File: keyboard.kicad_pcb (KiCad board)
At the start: 2 copper layers, 285 x 94.6 mm, 205 parts, among them J1 USB_OTG, K1 Jumper_NO_Small, P1 SWD, P2 BATT, U1 nrf51822-02, U2 CH554T, U3 TP4057, U4 XC6206P30

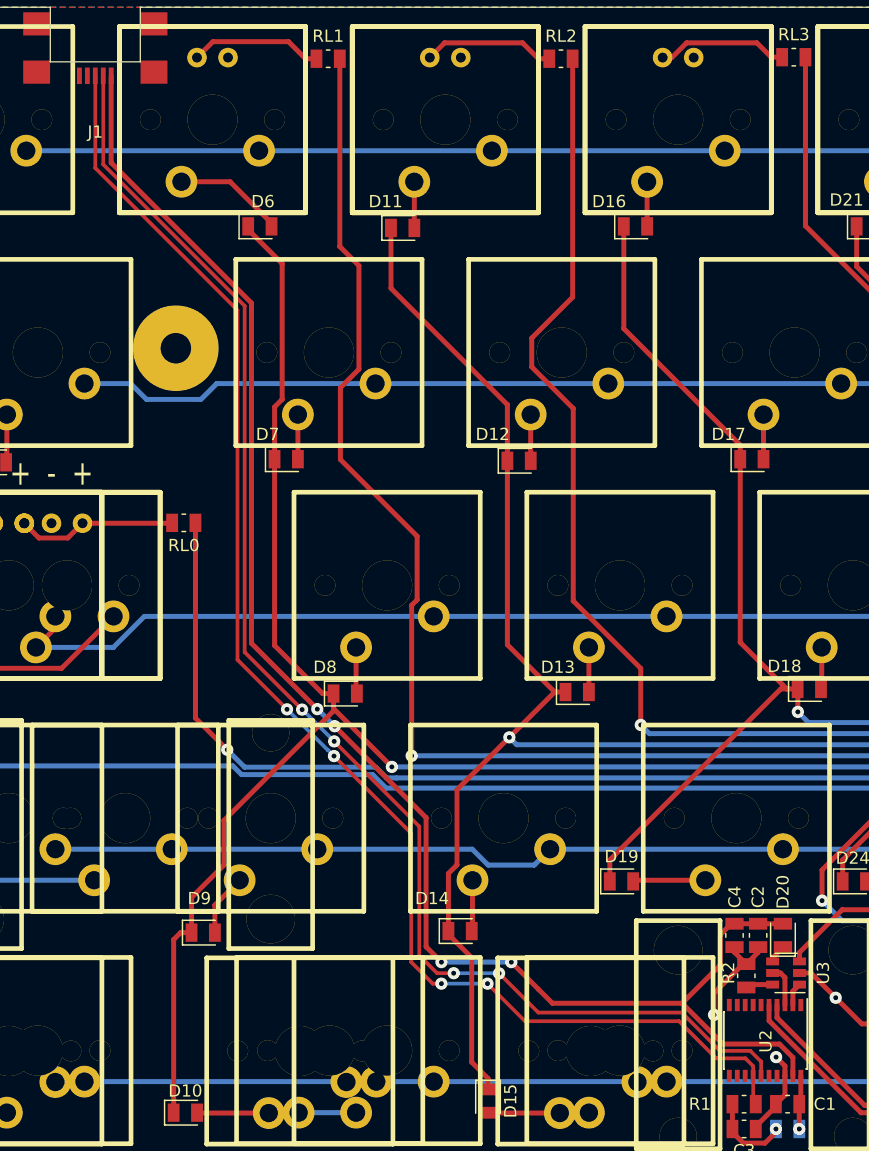
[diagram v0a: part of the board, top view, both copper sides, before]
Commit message: 应该是改了些布线方面的问题
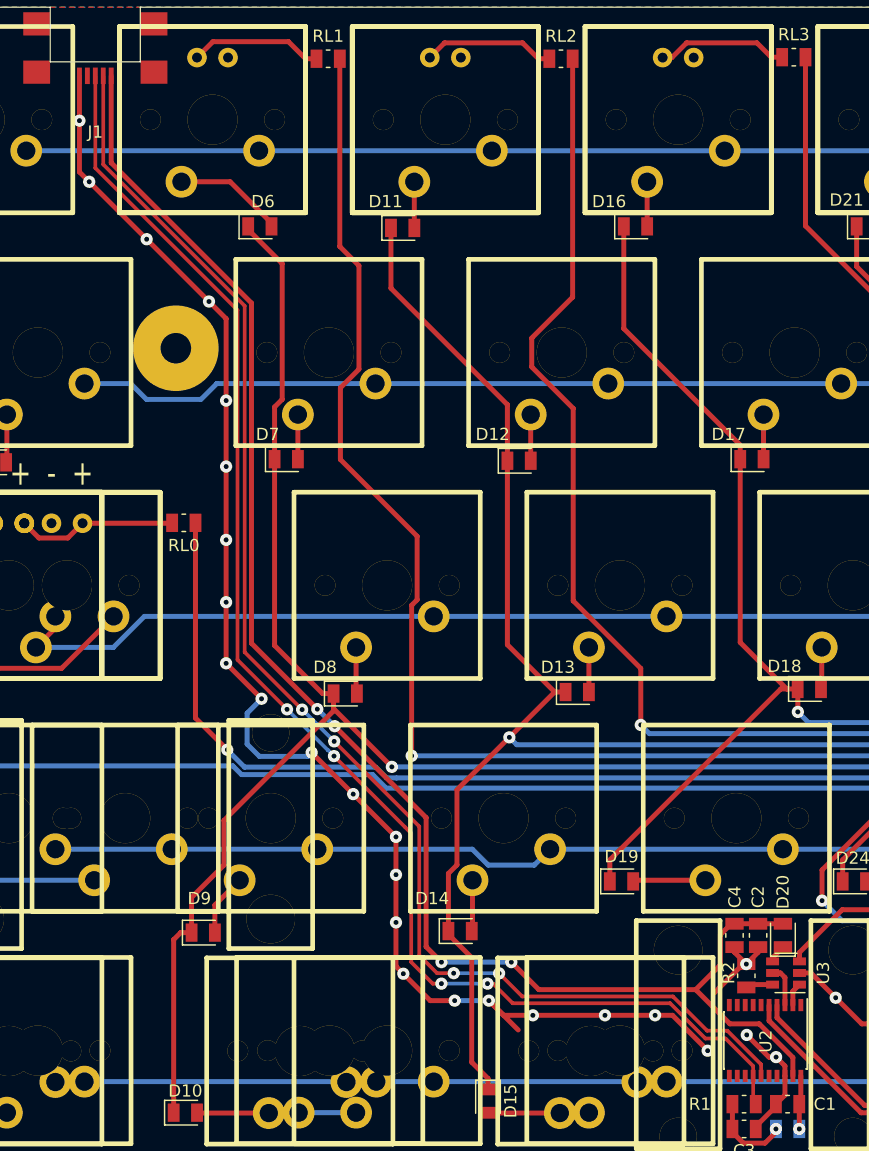
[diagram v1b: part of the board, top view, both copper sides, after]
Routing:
- net GND: track 83.6 -> 204.3 mm, vias 5 -> 28
- net VCC: track 129.6 -> 128.1 mm

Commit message: 替换接口为Type-C
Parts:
- added R5: 5.1K, Resistor_SMD:R_0805_2012Metric, B.Cu at (74.2, 69.6)
- added R6: 5.1K, Resistor_SMD:R_0805_2012Metric, B.Cu at (78.9, 75.4)
- added TP1: TP, TestPoint:TestPoint_Pad_D1.0mm, B.Cu at (140.6, 146.9)
- added TP2: TP, TestPoint:TestPoint_Pad_D1.0mm, B.Cu at (143.8, 146.9)
- added TP3: TP, TestPoint:TestPoint_Pad_D1.0mm, B.Cu at (142.2, 146.9)
- C1, C3, D20, P1, R1, R2, U1, U2, U3: moved to B.Cu
- J1: value USB_OTG -> USB_C_Receptacle_USB2.0; footprint custom:USB_Micro-B_lowp -> Connector_USB:USB_C_Receptacle_Amphenol_12401610E4-2A; moved to B.Cu
- moved U1 17.9 mm to (179.4, 140.2), turned to 270 degrees
- moved C4 9.21 mm to (136.4, 149.2)
- moved C2 8.67 mm to (134.4, 149.2)
- moved P1 7.04 mm to (140.8, 153.4), turned to 270 degrees
- moved R1 3.62 mm to (137.6, 154.2), turned to 180 degrees
- moved C3 3.62 mm to (137.6, 156.4), turned to 180 degrees
- moved C1 3.59 mm to (134.0, 154.2), turned to 0 degrees
- moved K1 3.59 mm to (134.0, 156.4), turned to 180 degrees
- moved R2 3.44 mm to (133.8, 140.4)
- moved U3 3.39 mm to (136.4, 140.4), turned to 270 degrees
- moved J1 2.73 mm to (81.0, 68.2), turned to 0 degrees
- moved D20 2.25 mm to (139.4, 140.4)
- moved G*** 0.64 mm to (226.0, 151.0)
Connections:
- U1 pad 32: TXD -> MOSI
- U1 pad 33: RXD -> MISO
- U1 pad 34: Net-(U1-Pad34) -> CLK
- U2 pad 4: RXD -> MOSI
- U2 pad 5: TXD -> MISO
- U2 pad 7: Net-(U2-Pad7) -> CLK
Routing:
- net GND: track 204.3 -> 286.9 mm, vias 28 -> 30
- net MOSI: track 0.00 -> 47.8 mm
- net MISO: track 0.00 -> 45.3 mm
- net CLK: track 0.00 -> 41.6 mm
- net /row3: track 359.3 -> 319.6 mm
- net RXD: track 35.9 -> 0.00 mm
- net TXD: track 35.5 -> 0.00 mm
- net VCC: track 128.1 -> 158.1 mm, vias 4 -> 6
- net /col1: track 177.6 -> 198.3 mm, vias 2 -> 3
- net UD_N: track 115.3 -> 134.3 mm
- net /caps_led: track 99.5 -> 118.1 mm, vias 2 -> 3
- net /col6: track 79.4 -> 97.9 mm, vias 0 -> 1
- net /led3: track 87.0 -> 105.0 mm, vias 2 -> 3
- net /row4: track 332.8 -> 314.8 mm
- net /col4: track 108.9 -> 126.8 mm, vias 2 -> 3
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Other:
- net class DATA: clearance 0.2032 -> 0.15; trace_width 0.3048 -> 0.25; via_dia 1 -> 0.7
- rule via_min_drill: 0.4 -> 0.3
- rule via_min_size: 1 -> 0.6
- board text added: "Last Order"
- board text added: "Lot60-BLE Rev.C ©2019 Lotlab"
- board text removed: "Lot60-BLE Rev.A ©2018 Lotlab"

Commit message: 使用52810替换51822
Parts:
- removed LED4, LED5: LED, MX1A:MX1A-led
- removed RL4, RL5: R, Resistor_SMD:R_0805_2012Metric
- added C8: 10uF, Capacitor_SMD:C_0805_2012Metric, F.Cu at (137.9, 149.4)
- added J2: -, Connector_PinSocket_2.54mm:PinSocket_1x05_P2.54mm_Vertical, F.Cu at (63.9, 98.6)
- added J3: -, Connector_PinSocket_2.54mm:PinSocket_1x05_P2.54mm_Vertical, F.Cu at (154.3, 157.5)
- added JP1: Jumper, Jumper:SolderJumper-2_P1.3mm_Bridged2Bar_Pad1.0x1.5mm, B.Cu at (143.8, 150.0)
- added TP4: TP, TestPoint:TestPoint_Pad_D1.0mm, B.Cu at (140.6, 144.5)
- added TP5: TP, TestPoint:TestPoint_Pad_D1.0mm, B.Cu at (139.1, 144.5)
- C1, C3, K1, P1, R1: moved to F.Cu
- C4: value 1uF -> 0.1uF
- D1, D10, D11, D12, D13, D14, D15, D16, D17, D18, D19, D2, D21, D22, D23, D24, D26, D27, D28, D29, D3, D30, D31, D32, D33, D34, D36, D37, D38, D39, D4, D41, D42, D43, D44, D46, D47, D48, D49, D5, D50, D51, D52, D53, D54, D55, D56, D57, D58, D59, D6, D60, D61, D62, D63, D64, D65, D66, D67, D68, D69, D7, D70, D8, D9, P2, RL0: moved to B.Cu
- RL1, RL2, RL3: value R -> 4.7K; moved to B.Cu
- U1: value nrf51822-02 -> nRF52810-ND04C; footprint custom:nRF51822-02 -> Customv2:nRF52810-ND04C
- moved P1 31.5 mm to (172.1, 157.5)
- moved RL1 27.2 mm to (76.5, 82.7)
- moved D30 24.8 mm to (178.6, 155.1)
- moved D29 20.0 mm to (181.4, 136.9)
- moved RL2 19.1 mm to (99.9, 68.7)
- moved LED3 19.1 mm to (109.5, 73.8)
- moved LED2 19.1 mm to (90.5, 73.8)
- moved LED1 19.0 mm to (71.4, 73.8)
- moved RL3 19.0 mm to (119.0, 68.7)
- moved U1 8.80 mm to (174.1, 147.2), turned to 180 degrees
- moved R2 4.09 mm to (133.6, 144.5), turned to 180 degrees
- moved D6 3.64 mm to (90.7, 82.7)
- moved D15 1.70 mm to (113.1, 155.8), turned to 90 degrees
- moved R6 1.56 mm to (78.9, 77.0)
- moved D20 1.45 mm to (138.5, 141.5)
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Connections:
- RL0 pad 1: /caps_led -> /caps
- U1 pad 1: 3V3 -> GND
- U1 pad 10: /col7 -> /row4
- U1 pad 11: GND -> /row5
- U1 pad 12: /led5 -> /col7
- U1 pad 13: /col6 -> ADC1
- U1 pad 14: /led4 -> /col8
- U1 pad 15: /col5 -> /col9
- U1 pad 16: /led3 -> /col10
- U1 pad 17: /col4 -> /col11
- U1 pad 18: /led2 -> /col12
- U1 pad 19: /col3 -> /col13
- U1 pad 2: /col14 -> 3V3
- U1 pad 20: /led1 -> /col14
- U1 pad 21: DIO -> /GPIO0
- U1 pad 22: DCLK -> /col6
- U1 pad 23: /col2 -> /col5
- U1 pad 24: /caps_led -> /col4
- U1 pad 25: /col1 -> /col3
- U1 pad 26: Net-(U1-Pad26) -> /col2
- U1 pad 27: GND -> /col1
- U1 pad 28: Net-(U1-Pad28) -> DIO
- U1 pad 29: GND -> DCLK
- U1 pad 3: /col13 -> /caps
- U1 pad 30: GND -> CLK
- U1 pad 31: GND -> MISO
- U1 pad 32: MOSI -> /GPIO2
- U1 pad 33: MISO -> /GPIO1
- U1 pad 4: ADC1 -> /led1
- U1 pad 5: /col12 -> /led2
- U1 pad 6: /col11 -> /led3
- U1 pad 7: /col10 -> /row1
- U1 pad 8: /col9 -> /row2
- U1 pad 9: /col8 -> /row3
- U2 pad 10: Net-(U2-Pad10) -> D_RX
- U2 pad 11: Net-(U2-Pad11) -> CHRG
- U2 pad 12: Net-(U2-Pad12) -> STBY
- U2 pad 2: CHRG -> Net-(U2-Pad2)
- U2 pad 3: STBY -> MOSI
- U2 pad 4: MOSI -> MISO
- U2 pad 5: MISO -> CLK
- U2 pad 7: CLK -> Net-(U2-Pad7)
- U2 pad 9: Net-(U2-Pad9) -> D_TX
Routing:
- net /caps_led: track 118.1 -> 0.00 mm, vias 3 -> 0
- net /caps: track 0.00 -> 103.4 mm, vias 0 -> 2
- net /led4: track 95.3 -> 0.00 mm, vias 1 -> 0
- net /led5: track 94.3 -> 0.00 mm, vias 3 -> 0
- net /row1: track 422.4 -> 354.1 mm, vias 1 -> 0
- net /row5: track 385.8 -> 438.6 mm, vias 0 -> 3
- net GND: track 286.9 -> 336.0 mm, vias 30 -> 7
- net MOSI: track 47.8 -> 16.4 mm
- net /GPIO0: track 0.00 -> 25.3 mm
- net /GPIO2: track 0.00 -> 24.8 mm
- net Net-(D30-Pad2): track 44.8 -> 22.7 mm
- net DIO: track 26.2 -> 4.82 mm
- net /row3: track 319.6 -> 340.8 mm, vias 2 -> 0
- net DCLK: track 21.6 -> 3.68 mm
- net /row4: track 314.8 -> 332.0 mm, vias 1 -> 0
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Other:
- board text added: "+ -"
- board text added: "3V3"
- board text added: "BATT"
- board text added: "DCLK"
- board text added: "DIO"
- board text added: "GND"
- board text added: "GPIO0"
- board text added: "GPIO1"
- board text added: "GPIO2"

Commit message: 微调布线
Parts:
- moved D30 2.98 mm to (176.0, 156.5), turned to 90 degrees
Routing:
- net GND: track 336.0 -> 340.9 mm, vias 7 -> 8
- net Net-(D30-Pad2): track 22.7 -> 26.4 mm
- net /GPIO0: track 25.3 -> 24.0 mm, vias 0 -> 1
- net MISO: track 38.8 -> 39.9 mm
- net CLK: track 39.2 -> 40.3 mm
- net /GPIO2: track 24.8 -> 25.9 mm
- net /row5: track 438.6 -> 439.7 mm
- net 3V3: track 86.8 -> 87.4 mm
- net /col6: track 87.0 -> 86.9 mm, vias 2 -> 0

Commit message: 更换type-c接口的封装
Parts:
- J1: footprint Connector_USB:USB_C_Receptacle_Amphenol_12401610E4-2A -> Customv2:USB_C_SIMPLE_ONBOARD
- moved R5 10.3 mm to (82.7, 76.6), turned to 90 degrees
- moved J1 3.63 mm to (80.9, 64.6)
- moved R6 0.34 mm to (78.9, 76.6), turned to 90 degrees
- renumbered HOLE to HOLE1, HOLE to HOLE2, HOLE to HOLE3, MXST to MXST1, MXST to MXST10, MXST to MXST11, MXST to MXST12, MXST to MXST13, MXST to MXST14, MXST to MXST15, MXST to MXST2, MXST to MXST3, MXST to MXST4, MXST to MXST5, MXST to MXST6, MXST to MXST7, MXST to MXST8, MXST to MXST9
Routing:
- net UD_P: track 144.9 -> 150.9 mm, vias 1 -> 3
- net Net-(J1-PadB5): track 7.76 -> 3.85 mm
- net UD_N: track 144.4 -> 147.8 mm
- net /row3: track 340.8 -> 344.2 mm
- net VCC: track 158.1 -> 155.9 mm
- net GND: track 340.9 -> 339.7 mm
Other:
- outline, holes or cut-outs redrawn

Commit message: 增加电容，更改type-c封装为非沉板式
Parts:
- added C9: 1uF, Capacitor_SMD:C_0805_2012Metric, F.Cu at (214.6, 143.9)
- C5: moved to B.Cu
- J1: footprint Customv2:USB_C_SIMPLE_ONBOARD -> Customv2:USB_C_SIMPLE
- RL1, RL2, RL3: value 4.7K -> 300
- moved C5 79.4 mm to (135.5, 137.8)
- moved RL0 3.76 mm to (88.1, 110.6)
- moved J1 1.00 mm to (80.9, 63.6)
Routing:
- net /caps: track 103.4 -> 99.7 mm
- net GND: track 339.7 -> 342.6 mm, vias 8 -> 17
- net BATT: track 96.1 -> 98.7 mm
- net Net-(DC1-Pad1): track 13.1 -> 14.7 mm
- net VCC: track 155.9 -> 156.1 mm, vias 4 -> 2
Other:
- outline, holes or cut-outs redrawn

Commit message: 增加RGB LED
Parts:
- removed the G*** at (226.0, 151.0)
- added D25: LED_CRGB, LED_SMD:LED_RGB_1210, F.Cu at (71.4, 68.3)
- added G***: LOGO, Customv2:last_order, B.Cu at (228.9, 149.8)
- moved RL1 22.5 mm to (98.1, 76.4), turned to 270 degrees
- moved LED3 19.1 mm to (128.6, 73.8)
- moved LED2 19.1 mm to (109.5, 73.8)
- moved LED1 19.0 mm to (90.5, 73.8)
- moved RL2 7.91 mm to (101.9, 76.4), turned to 270 degrees
- moved RL3 7.70 mm to (120.0, 76.4), turned to 270 degrees
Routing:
- net 3V3: track 87.4 -> 236.9 mm, vias 1 -> 4
- net Net-(D25-Pad1): track 10.8 -> 70.1 mm
- net Net-(D25-Pad4): track 10.7 -> 46.3 mm
- net /led2: track 135.3 -> 121.1 mm
- net Net-(D25-Pad3): track 17.2 -> 28.3 mm
- net /led1: track 132.6 -> 122.6 mm, vias 2 -> 4
- net /led3: track 106.0 -> 97.4 mm
- net GND: track 342.6 -> 343.3 mm
- net /col5: track 119.8 -> 119.2 mm
- net /col2: track 177.2 -> 176.7 mm
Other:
- board text added: "Uchidome image © Pixiv ID: 50660802"
- board text removed: "id: 52846813"
